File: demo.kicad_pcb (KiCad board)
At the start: 4 copper layers, 0 parts

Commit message: V1.0.2
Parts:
- added C1: 10uF, Capacitor_SMD:C_0603_1608Metric, F.Cu at (110.6, 86.4)
- added C10: 10pF, Capacitor_SMD:C_0402_1005Metric, F.Cu at (132.7, 94.5)
- added C11: 10pF, Capacitor_SMD:C_0402_1005Metric, F.Cu at (135.0, 89.5)
- added C2: 100nF, Capacitor_SMD:C_0402_1005Metric, F.Cu at (110.1, 87.8)
- added C3: 22uF, Capacitor_SMD:C_0603_1608Metric, F.Cu at (115.5, 95.7)
- added C4: 100nF, Capacitor_SMD:C_0402_1005Metric, F.Cu at (117.6, 95.7)
- added C5: 100nF, Capacitor_SMD:C_0402_1005Metric, F.Cu at (121.4, 96.5)
- added C6: 100nF, Capacitor_SMD:C_0402_1005Metric, F.Cu at (130.3, 96.9)
- added C7: 100nF, Capacitor_SMD:C_0402_1005Metric, F.Cu at (132.7, 89.5)
- added C8: 100nF, Capacitor_SMD:C_0402_1005Metric, F.Cu at (121.8, 87.6)
- added C9: 100nF, Capacitor_SMD:C_0402_1005Metric, F.Cu at (135.0, 88.5)
- added D1: LED_RED, LED_SMD:LED_0402_1005Metric, F.Cu at (115.5, 86.3)
- added D2: LED_GREEN, LED_SMD:LED_0402_1005Metric, F.Cu at (116.5, 86.3)
- added J1: USB_C_Receptacle, Library:USB_C_Receptacle_typecf 双排 SMT六孔, F.Cu at (104.0, 92.5)
- added J2: Conn_02x05_Odd_Even, Connector_PinHeader_2.54mm:PinHeader_2x05_P2.54mm_Horizontal, F.Cu at (137.9, 87.4)
- added J3: Conn_01x04, Connector_PinHeader_1.27mm:PinHeader_1x04_P1.27mm_Vertical, F.Cu at (118.9, 98.3)
- added Q1: S9013, Package_TO_SOT_SMD:SOT-23, F.Cu at (111.9, 97.6)
- added R1: 100K, Resistor_SMD:R_0402_1005Metric, F.Cu at (110.1, 89.1)
- added R10: 22, Resistor_SMD:R_0402_1005Metric, F.Cu at (135.0, 94.5)
- added R11: 22, Resistor_SMD:R_0402_1005Metric, F.Cu at (135.0, 96.5)
- added R12: 22, Resistor_SMD:R_0402_1005Metric, F.Cu at (135.0, 95.5)
- added R13: 22, Resistor_SMD:R_0402_1005Metric, F.Cu at (135.0, 97.5)
- added R14: 22, Resistor_SMD:R_0402_1005Metric, F.Cu at (119.7, 95.7)
- added R15: 22, Resistor_SMD:R_0402_1005Metric, F.Cu at (118.7, 95.7)
- added R16: 100K, Resistor_SMD:R_0402_1005Metric, F.Cu at (135.0, 87.5)
- added R17: 100K, Resistor_SMD:R_0402_1005Metric, F.Cu at (132.7, 97.6)
- added R18: 100, Resistor_SMD:R_0402_1005Metric, F.Cu at (119.7, 86.3)
- added R19: 10K, Resistor_SMD:R_0402_1005Metric, F.Cu at (132.7, 96.5)
- added R2: 10, Resistor_SMD:R_0402_1005Metric, F.Cu at (110.1, 92.5)
- added R20: 10K, Resistor_SMD:R_0402_1005Metric, F.Cu at (132.7, 95.5)
- added R21: 100, Resistor_SMD:R_0402_1005Metric, F.Cu at (118.6, 86.3)
- added R22: 4K7, Resistor_SMD:R_0402_1005Metric, F.Cu at (132.7, 87.5)
- added R23: 4K7, Resistor_SMD:R_0402_1005Metric, F.Cu at (132.7, 88.5)
- added R3: 10, Resistor_SMD:R_0402_1005Metric, F.Cu at (110.1, 90.2)
- added R4: 1.5K, Resistor_SMD:R_0402_1005Metric, F.Cu at (110.1, 91.4)
- added R5: 10K, Resistor_SMD:R_0402_1005Metric, F.Cu at (110.1, 93.7)
- added R6: 36K, Resistor_SMD:R_0402_1005Metric, F.Cu at (110.1, 94.9)
- added R7: 100, Resistor_SMD:R_0402_1005Metric, F.Cu at (110.1, 96.0)
- added R8: 100, Resistor_SMD:R_0402_1005Metric, F.Cu at (114.4, 86.3)
- added R9: 100, Resistor_SMD:R_0402_1005Metric, F.Cu at (117.5, 86.3)
- added U1: AMS1117-3.3, Package_TO_SOT_SMD:SOT-223-3_TabPin2, F.Cu at (115.8, 91.0)
- added U2: STM32F103C8Tx, Package_QFP:LQFP-48_7x7mm_P0.5mm, F.Cu at (126.0, 92.2)
- added Y1: 8M, Crystal:Crystal_SMD_3225-4Pin_3.2x2.5mm, F.Cu at (133.8, 92.0)
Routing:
- net +5V: track 17.1 -> 63.0 mm, vias 0 -> 1
- net /T_Rx: track 0.00 -> 21.1 mm, vias 0 -> 1
- net GND: track 9.07 -> 29.0 mm, vias 0 -> 12
- net T_JTCK: track 19.2 -> 0.00 mm
- net /T_JTCK: track 0.00 -> 18.4 mm, vias 0 -> 3
- net Net-(J4-CC1): track 16.8 -> 0.00 mm
- net T_NRST: track 16.4 -> 0.00 mm
- net /T_SWO: track 0.00 -> 16.4 mm, vias 0 -> 2
- net SWO: track 16.2 -> 0.00 mm
- net /T_NRST: track 0.00 -> 15.2 mm, vias 0 -> 2
- net /T_Tx: track 0.00 -> 15.1 mm, vias 0 -> 1
- net /DP+: track 0.00 -> 14.5 mm, vias 0 -> 2
- net /RENUM: track 0.00 -> 14.5 mm, vias 0 -> 2
- net /DM-: track 0.00 -> 13.1 mm, vias 0 -> 2
- net STLINK_USB_DM-: track 13.1 -> 0.00 mm
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- added copper zone on In1.Cu, net +3V3
- added copper zone on In2.Cu, net GND
- removed copper zone on B.Cu, net GND
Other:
- board outline added: 45 x 15 mm
- board text added: "3.3V"
- board text added: "5V"
- board text added: "GND"
- board text added: "NRST"
- board text added: "RX"
- board text added: "STLINK V2.1"
- board text added: "SWCLK"
- board text added: "SWDIO"
- board text added: "SWO"
- board text added: "TX"

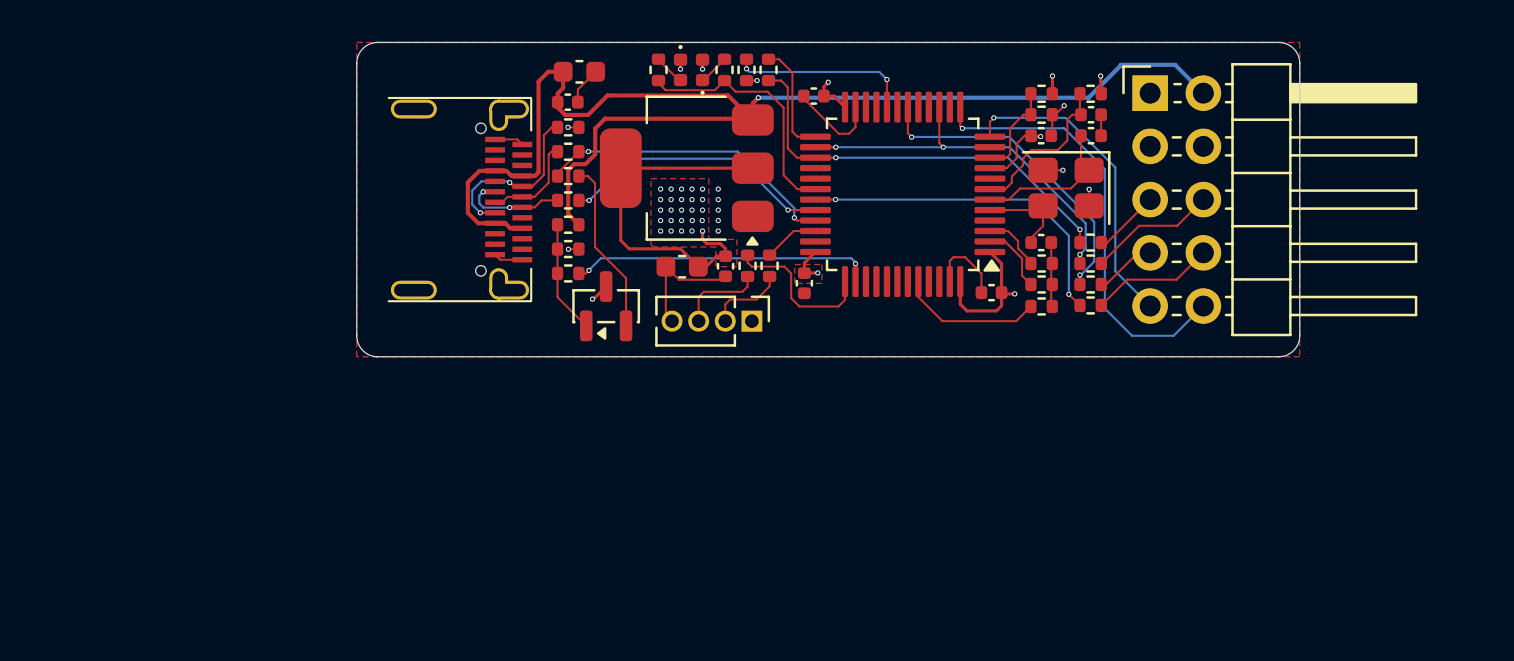
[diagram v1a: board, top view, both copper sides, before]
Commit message: modify hole size at min 0.3mm
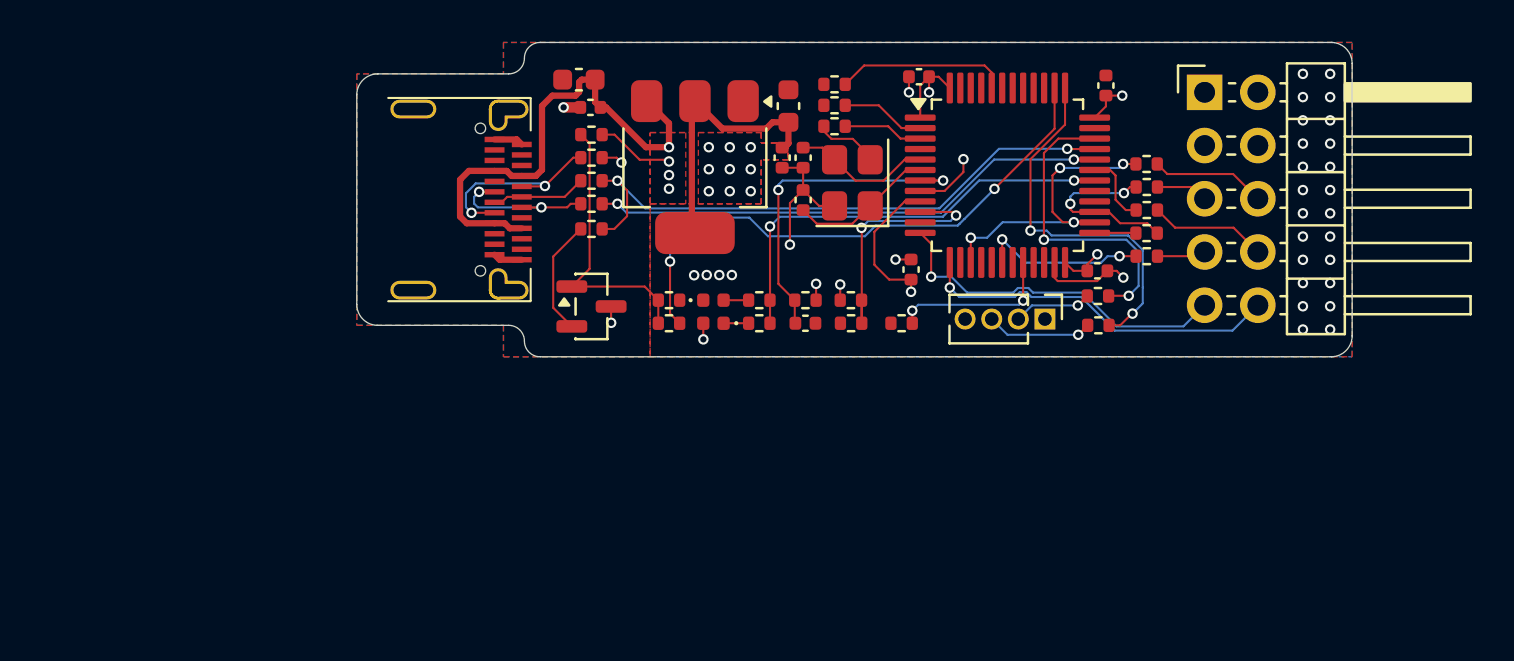
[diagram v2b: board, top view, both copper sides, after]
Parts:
- moved R18 19.7 mm to (137.7, 94.1), turned to 0 degrees
- moved R15 17.0 mm to (135.4, 98.5), turned to 180 degrees
- moved C9 16.9 mm to (121.4, 98.4)
- moved R16 16.8 mm to (121.4, 97.3)
- moved R14 15.7 mm to (135.4, 97.1), turned to 180 degrees
- moved R17 14.5 mm to (122.8, 87.0), turned to 0 degrees
- moved R21 14.2 mm to (126.0, 98.4), turned to 0 degrees
- moved C11 14.1 mm to (121.3, 92.5), turned to -90 degrees
- moved J3 14.0 mm to (132.8, 98.2)
- moved R23 13.5 mm to (123.6, 98.4), turned to 0 degrees
- moved R22 13.4 mm to (123.6, 97.3), turned to 180 degrees
- moved R19 13.1 mm to (122.8, 88.0), turned to 0 degrees
- moved R9 12.2 mm to (119.2, 98.4), turned to 0 degrees
- moved D2 12.1 mm to (117.0, 98.4), turned to 180 degrees
- moved C10 12.1 mm to (121.3, 90.5), turned to 90 degrees
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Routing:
- net +5V: track 63.0 -> 27.5 mm, vias 1 -> 4
- net /DP+: track 14.5 -> 28.6 mm
- net /T_SWO: track 16.4 -> 3.45 mm, vias 2 -> 0
- net /RENUM: track 14.5 -> 27.4 mm
- net /STM_JTMS: track 2.66 -> 14.9 mm, vias 0 -> 2
- net /DM-: track 13.1 -> 24.7 mm
- net /T_JTMS: track 20.1 -> 8.55 mm
- net /STM_JTCK: track 7.57 -> 17.8 mm, vias 0 -> 2
- net /LED_STLINK: track 12.0 -> 21.0 mm, vias 0 -> 2
- net /NRST: track 7.78 -> 16.0 mm, vias 0 -> 2
- net Net-(Q1-B): track 5.39 -> 13.3 mm
- net Net-(U2-PA0): track 4.53 -> 12.2 mm, vias 0 -> 2
- net /T_NRST: track 15.2 -> 8.08 mm
- net GND: track 29.0 -> 23.4 mm, vias 12 -> 35
- net /T_JTCK: track 18.4 -> 14.6 mm, vias 3 -> 4
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- added copper zone on F.Cu, net +5V
- added copper zone on In1.Cu, net +5V
- added copper zone on B.Cu, net GND
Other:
- board size 45 x 15 mm -> 47.5 x 15 mm
- board text added: "3V3"
- board text added: "STLINK V2.1(type-c版本) 2025-11-26 V1.0.2"
- board text removed: "3.3V"
- board text removed: "STLINK V2.1"

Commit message: 1.3*3.8(cm^2) relayout
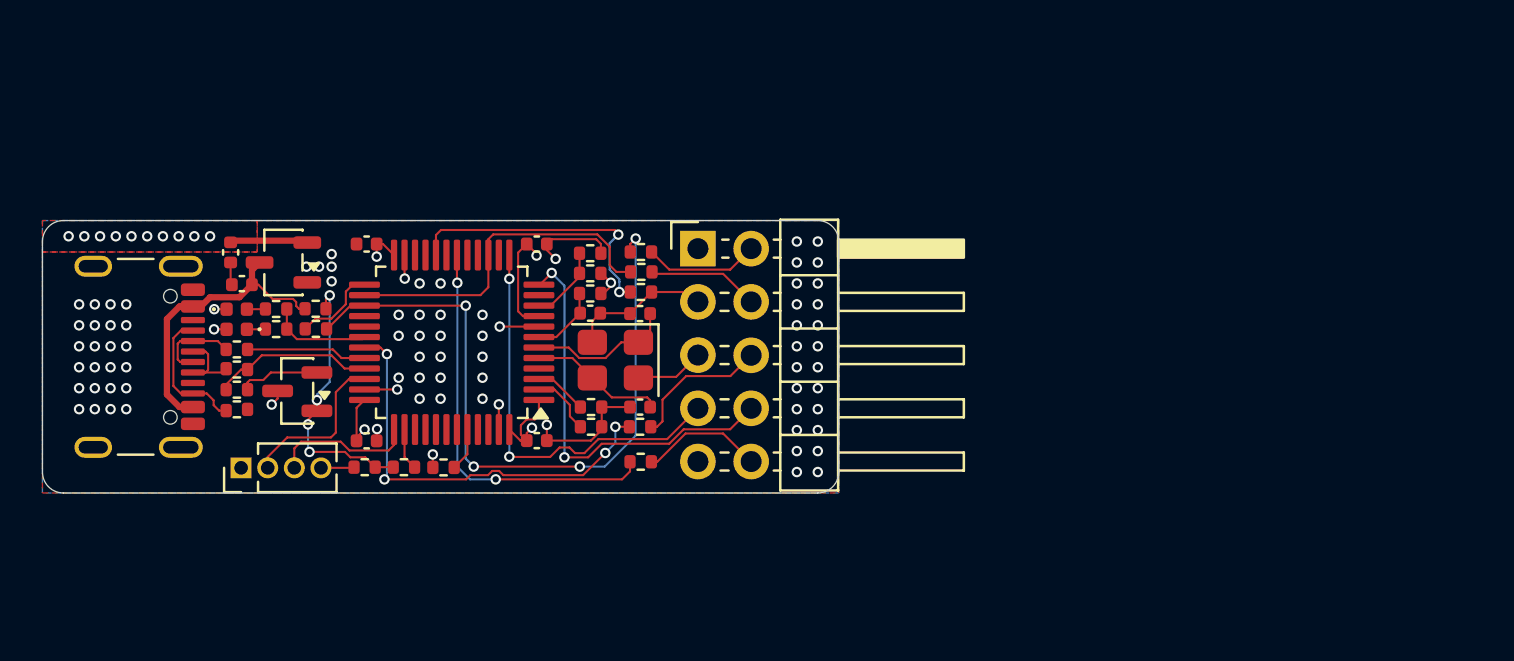
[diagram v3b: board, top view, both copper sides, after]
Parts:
- removed C10, C11: 10pF, Capacitor_SMD:C_0402_1005Metric
- removed R22, R23: 4K7, Resistor_SMD:R_0402_1005Metric
- C1: value 10uF -> 1uF; footprint Capacitor_SMD:C_0603_1608Metric -> Capacitor_SMD:C_0402_1005Metric
- C2: value 100nF -> 1uF
- C3: value 22uF -> 100nF; footprint Capacitor_SMD:C_0603_1608Metric -> Capacitor_SMD:C_0402_1005Metric
- C8, C9: value 100nF -> 10pF
- J1: value USB_C_Receptacle -> USB_C_Receptacle_USB2.0_16P; footprint Library:USB_C_Receptacle_typecf 双排 SMT六孔 -> Connector_USB:USB_C_Receptacle_GCT_USB4105-xx-A_16P_TopMnt_Horizontal
- R14, R15: value 22 -> 100K
- R16: value 100K -> 100
- R17: value 100K -> 10K
- R18: value 100 -> 10K
- R19: value 10K -> 100
- R20: value 10K -> 4K7
- R21: value 100 -> 4K7
- U1: value AMS1117-3.3 -> XC6206P332MR; footprint Package_TO_SOT_SMD:SOT-223-3_TabPin2 -> Package_TO_SOT_SMD:SOT-23-3
- U2: value STM32F103C8Tx -> STM32F103CBT6
- moved J3 39.0 mm to (94.5, 105.3), turned to 90 degrees
- moved C6 34.9 mm to (100.5, 94.6), turned to 180 degrees
- moved R15 32.0 mm to (104.1, 105.3), turned to 0 degrees
- moved R18 27.8 mm to (111.2, 102.4), turned to 180 degrees
- moved U2 27.7 mm to (104.5, 99.3), turned to 180 degrees
- moved C5 27.2 mm to (100.5, 104.0), turned to 0 degrees
- moved C7 26.9 mm to (111.1, 97.9), turned to 0 degrees
- moved R13 26.3 mm to (113.5, 103.3)
- moved R11 26.1 mm to (113.5, 105.0)
- moved J2 25.3 mm to (116.3, 94.8)
- moved R12 24.7 mm to (113.6, 96.0)
- moved R10 24.3 mm to (113.6, 95.0)
- moved R14 24.2 mm to (111.1, 97.0)
- moved R16 23.4 mm to (98.0, 98.7), turned to 0 degrees
- moved R8 23.1 mm to (96.2, 97.7)
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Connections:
- C2 pad 1: +5V -> +3V3
- C7 pad 1: +3V3 -> /NRST
- C8 pad 1: +3V3 -> GND
- C8 pad 2: GND -> Net-(U2-PD0)
- C9 pad 1: /NRST -> GND
- C9 pad 2: GND -> Net-(U2-PD1)
- J2 pad 10: /T_Rx -> Net-(J2-Pin_10)
- J2 pad 2: +5V -> Net-(J2-Pin_2)
- J2 pad 4: GND -> Net-(J2-Pin_4)
- J2 pad 5: Net-(J2-Pin_5) -> GND
- J2 pad 7: Net-(J2-Pin_7) -> /T_Rx
- J2 pad 8: Net-(J2-Pin_8) -> /T_Tx
- J2 pad 9: /T_Tx -> GND
- J3 pad 2: Net-(J3-Pin_2) -> /STM_JTMS
- J3 pad 3: Net-(J3-Pin_3) -> /STM_JTCK
- R10 pad 1: Net-(J2-Pin_5) -> Net-(J2-Pin_2)
- R11 pad 1: Net-(J2-Pin_7) -> Net-(J2-Pin_10)
- R12 pad 2: Net-(J2-Pin_6) -> Net-(J2-Pin_4)
- R13 pad 2: Net-(J2-Pin_8) -> Net-(J2-Pin_6)
- R14 pad 1: /STM_JTMS -> +3V3
- R14 pad 2: Net-(J3-Pin_2) -> /NRST
- R15 pad 1: /STM_JTCK -> GND
- R15 pad 2: Net-(J3-Pin_3) -> /BOOT0
- R16 pad 1: +3V3 -> Net-(U2-PB12)
- R16 pad 2: /NRST -> /T_JTMS
- R17 pad 2: /BOOT0 -> Net-(U2-PC13)
- R18 pad 1: Net-(U2-PB12) -> GND
- R18 pad 2: /T_JTMS -> Net-(U2-PC14)
- R19 pad 2: Net-(U2-PC13) -> Net-(U2-PB2)
- R20 pad 1: GND -> Net-(U2-PA0)
- R20 pad 2: Net-(U2-PC14) -> +3V3
- R21 pad 2: Net-(U2-PB2) -> Net-(U2-PA0)
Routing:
- net /RENUM: track 27.4 -> 2.00 mm, vias 2 -> 0
- net /T_JTMS: track 8.55 -> 33.4 mm, vias 2 -> 4
- net /DP+: track 28.6 -> 7.69 mm, vias 2 -> 0
- net /DM-: track 24.7 -> 5.75 mm, vias 2 -> 0
- net /T_SWO: track 3.45 -> 20.6 mm, vias 0 -> 4
- net /LED_STLINK: track 21.0 -> 4.91 mm, vias 2 -> 0
- net +5V: track 27.5 -> 14.2 mm, vias 4 -> 0
- net /NRST: track 16.0 -> 3.39 mm, vias 2 -> 0
- net /T_NRST: track 8.08 -> 19.2 mm
- net /STM_JTCK: track 17.8 -> 6.84 mm, vias 2 -> 0
- net +3V3: track 31.4 -> 20.6 mm
- net Net-(U2-PA0): track 12.2 -> 3.63 mm, vias 2 -> 0
- net /STM_JTMS: track 14.9 -> 7.81 mm, vias 2 -> 0
- net GND: track 23.4 -> 30.5 mm, vias 35 -> 82
- net /BOOT0: track 8.24 -> 2.07 mm
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- added copper zone on In2.Cu, net +3V3
- added copper zone on In1.Cu, net GND
- removed copper zone on In1.Cu, net +3V3
- removed copper zone on F.Cu, net +5V
- removed copper zone on In1.Cu, net +5V
- removed copper zone on In2.Cu, net GND
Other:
- board size 47.5 x 15 mm -> 38 x 13 mm
- board text added: "+3v3"
- board text added: "2025-12-13"
- board text added: "STLLINK V2.1 (type-c)"
- board text added: "v1.0.3"
- board text removed: "3V3"
- board text removed: "5V"
- board text removed: "STLINK V2.1(type-c版本) 2025-11-26 V1.0.2"
